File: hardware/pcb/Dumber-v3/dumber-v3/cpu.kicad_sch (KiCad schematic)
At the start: 25 parts, among them J1 Conn_02x03_Odd_Even, J2 Conn_02x03_Odd_Even, J3 Conn_02x05_Odd_Even, J4 TE 1-84982-0, M1 Motor, M2 Motor, Q2 PMN52XP, U1 XBEE-3, U2 STM32F071CBTx, U7 A3909

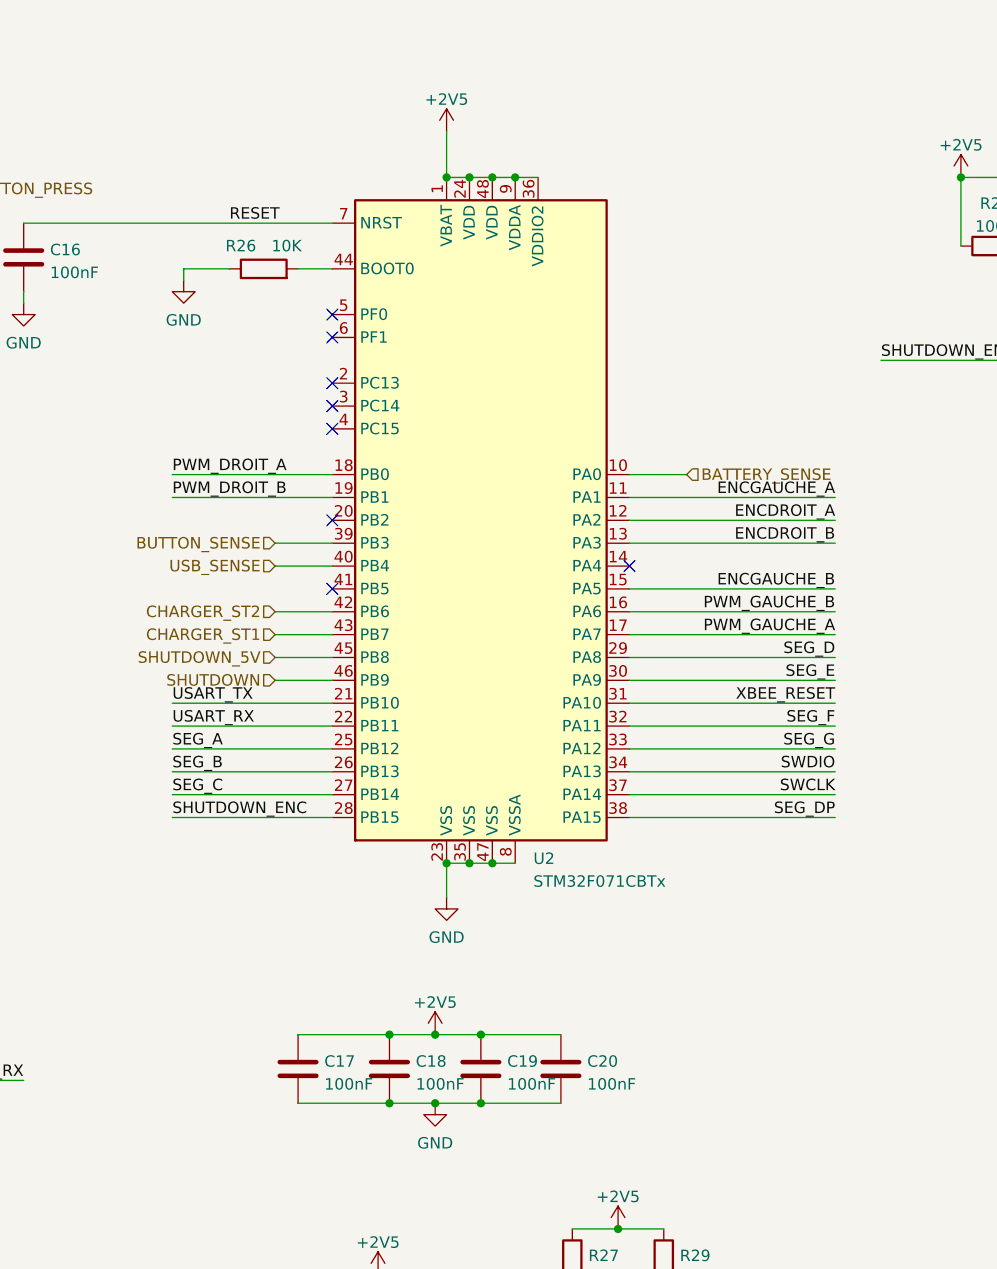
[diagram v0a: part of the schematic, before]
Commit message: Modifications after testing: func 11 needs more work.
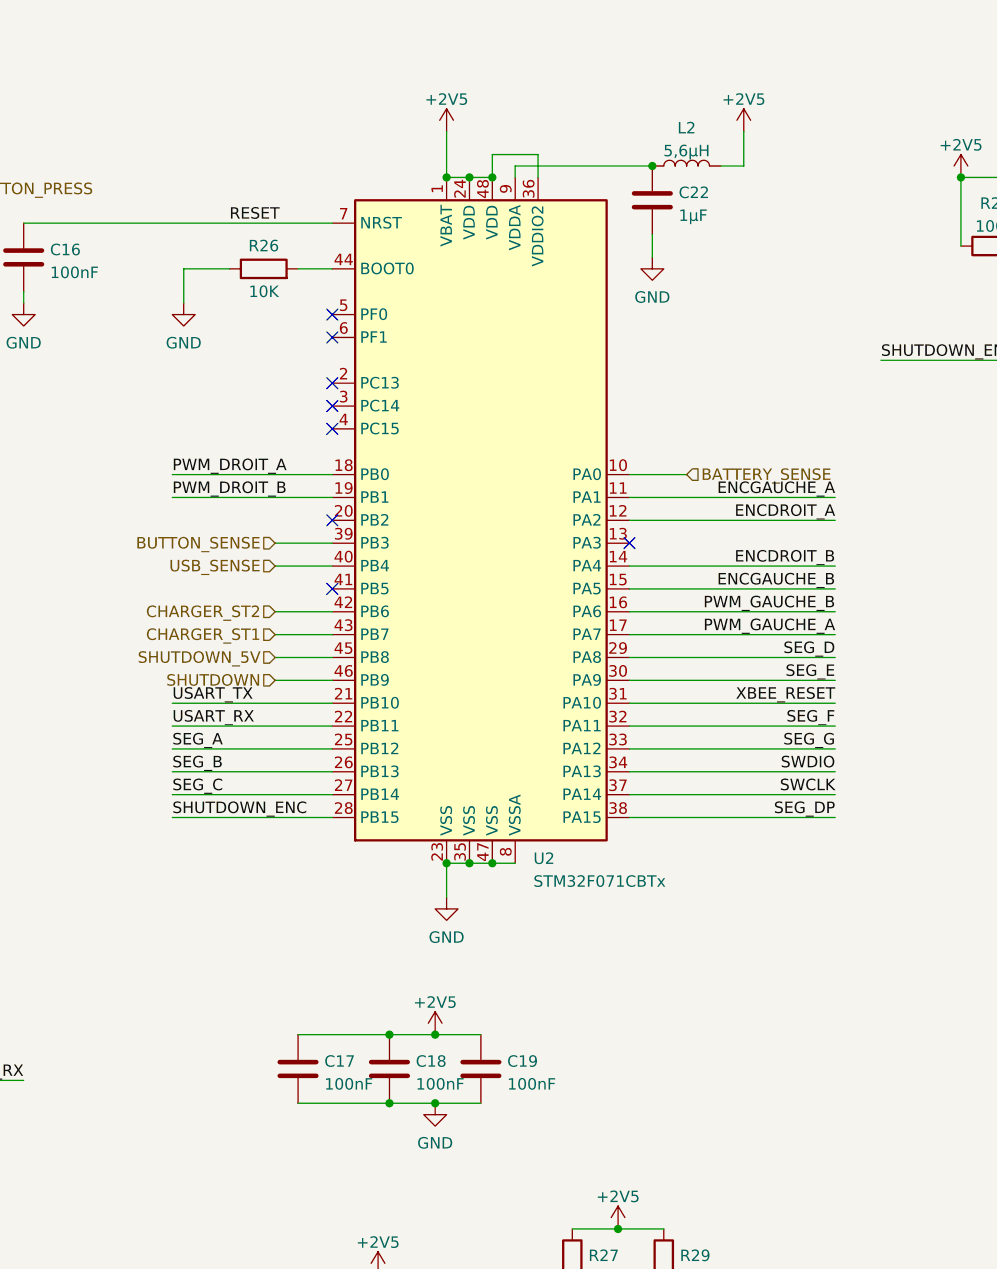
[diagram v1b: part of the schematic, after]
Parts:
- removed C20: 100nF, Capacitor_SMD:C_0805_2012Metric, symbol Device:C
- added C22: 1µF, Capacitor_SMD:C_0805_2012Metric, symbol Device:C
- added L2: 5,6µH, Inductor_SMD:L_1812_4532Metric, symbol Device:L
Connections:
- net +2V5: now also L2.2; no longer U2.9 (VDDA)
- net ENCDROIT_B: now also U2.14 (PA4); no longer U2.13 (PA3)
- net GND: now also C22.2
- new net: C22.1, L2.1, U2.9 (VDDA)
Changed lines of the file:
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@@
   (title_block
     (title "CPU + Com + Motors")
-    (date "2022-06-08")
-    (rev "1.0")
+    (date "2023-03-29")
+    (rev "2.1")
     (company "INSA - GEI")
   )
@@
   (junction (at 49.53 173.99) (diameter 0) (color 0 0 0 0)
   )
+  (junction (at 152.4 36.83) (diameter 0) (color 0 0 0 0)
+  )
   (junction (at 123.19 140.97) (diameter 0) (color 0 0 0 0)
   )
@@
   (junction (at 143.51 165.1) (diameter 0) (color 0 0 0 0)
   )
-  (junction (at 137.16 38.1) (diameter 0) (color 0 0 0 0)
-  )
   (junction (at 232.41 38.1) (diameter 0) (color 0 0 0 0)
   )
@@
   (junction (at 134.62 38.1) (diameter 0) (color 0 0 0 0)
   )
-  (junction (at 133.35 133.35) (diameter 0) (color 0 0 0 0)
-  )
-  (junction (at 133.35 140.97) (diameter 0) (color 0 0 0 0)
-  )
   (junction (at 128.27 133.35) (diameter 0) (color 0 0 0 0)
   )
@@
   )
   (no_connect (at 116.84 66.04))
-  (no_connect (at 149.86 81.28))
+  (no_connect (at 149.86 78.74))
   (no_connect (at 116.84 83.82))
   (no_connect (at 116.84 76.2))
@@
     (stroke (width 0) (type default) (color 0 0 0 0))
   )
+  (wire (pts (xy 134.62 38.1) (xy 134.62 35.56))
+    (stroke (width 0) (type default) (color 0 0 0 0))
+  )
   (wire (pts (xy 19.05 142.24) (xy 34.29 142.24))
     (stroke (width 0) (type default) (color 0 0 0 0))
@@
     (stroke (width 0) (type default) (color 0 0 0 0))
   )
+  (wire (pts (xy 139.7 35.56) (xy 139.7 38.1))
+    (stroke (width 0) (type default) (color 0 0 0 0))
+  )
   (wire (pts (xy 149.86 109.22) (xy 172.72 109.22))
     (stroke (width 0) (type default) (color 0 0 0 0))
@@
     (stroke (width 0) (type default) (color 0 0 0 0))
   )
+  (wire (pts (xy 134.62 35.56) (xy 139.7 35.56))
+    (stroke (width 0) (type default) (color 0 0 0 0))
+  )
+  (wire (pts (xy 162.56 33.02) (xy 162.56 36.83))
+    (stroke (width 0) (type default) (color 0 0 0 0))
+  )
   (wire (pts (xy 200.66 80.01) (xy 200.66 67.31))
     (stroke (width 0) (type default) (color 0 0 0 0))
   )
-  (wire (pts (xy 149.86 78.74) (xy 172.72 78.74))
-    (stroke (width 0) (type default) (color 0 0 0 0))
-  )
   (wire (pts (xy 64.77 138.43) (xy 82.55 138.43))
     (stroke (width 0) (type default) (color 0 0 0 0))
@@
     (stroke (width 0) (type default) (color 0 0 0 0))
   )
+  (wire (pts (xy 137.16 36.83) (xy 152.4 36.83))
+    (stroke (width 0) (type default) (color 0 0 0 0))
+  )
   (wire (pts (xy 217.17 45.72) (xy 234.95 45.72))
     (stroke (width 0) (type default) (color 0 0 0 0))
@@
     (stroke (width 0) (type default) (color 0 0 0 0))
   )
+  (wire (pts (xy 162.56 36.83) (xy 160.02 36.83))
+    (stroke (width 0) (type default) (color 0 0 0 0))
+  )
   (wire (pts (xy 266.7 92.71) (xy 266.7 96.52))
     (stroke (width 0) (type default) (color 0 0 0 0))
@@
     (stroke (width 0) (type default) (color 0 0 0 0))
   )
-  (wire (pts (xy 133.35 133.35) (xy 142.24 133.35))
-    (stroke (width 0) (type default) (color 0 0 0 0))
-  )
   (wire (pts (xy 54.61 39.37) (xy 54.61 69.85))
     (stroke (width 0) (type default) (color 0 0 0 0))
@@
     (stroke (width 0) (type default) (color 0 0 0 0))
   )
+  (wire (pts (xy 149.86 81.28) (xy 172.72 81.28))
+    (stroke (width 0) (type default) (color 0 0 0 0))
+  )
   (wire (pts (xy 129.54 33.02) (xy 129.54 38.1))
     (stroke (width 0) (type default) (color 0 0 0 0))
@@
     (stroke (width 0) (type default) (color 0 0 0 0))
   )
-  (wire (pts (xy 134.62 38.1) (xy 137.16 38.1))
-    (stroke (width 0) (type default) (color 0 0 0 0))
-  )
   (wire (pts (xy 201.93 38.1) (xy 232.41 38.1))
     (stroke (width 0) (type default) (color 0 0 0 0))
@@
     (stroke (width 0) (type default) (color 0 0 0 0))
   )
-  (wire (pts (xy 100.33 48.26) (xy 100.33 49.53))
+  (wire (pts (xy 100.33 48.26) (xy 100.33 52.07))
     (stroke (width 0) (type default) (color 0 0 0 0))
   )
@@
     (stroke (width 0) (type default) (color 0 0 0 0))
   )
-  (wire (pts (xy 133.35 140.97) (xy 142.24 140.97))
-    (stroke (width 0) (type default) (color 0 0 0 0))
-  )
   (wire (pts (xy 149.86 73.66) (xy 172.72 73.66))
     (stroke (width 0) (type default) (color 0 0 0 0))
@@
     (stroke (width 0) (type default) (color 0 0 0 0))
   )
+  (wire (pts (xy 152.4 44.45) (xy 152.4 46.99))
+    (stroke (width 0) (type default) (color 0 0 0 0))
+  )
   (wire (pts (xy 123.19 140.97) (xy 128.27 140.97))
     (stroke (width 0) (type default) (color 0 0 0 0))
   )
-  (wire (pts (xy 137.16 38.1) (xy 139.7 38.1))
-    (stroke (width 0) (type default) (color 0 0 0 0))
-  )
   (wire (pts (xy 113.03 48.26) (xy 116.84 48.26))
     (stroke (width 0) (type default) (color 0 0 0 0))
@@
     (stroke (width 0) (type default) (color 0 0 0 0))
   )
+  (wire (pts (xy 137.16 38.1) (xy 137.16 36.83))
+    (stroke (width 0) (type default) (color 0 0 0 0))
+  )
   (wire (pts (xy 232.41 29.21) (xy 234.95 29.21))
     (stroke (width 0) (type default) (color 0 0 0 0))
@@
     (stroke (width 0) (type default) (color 0 0 0 0))
   )
-  (label "ENCDROIT_B" (at 172.72 78.74 180)
+  (label "ENCDROIT_B" (at 172.72 81.28 180)
     (effects (font (size 1.27 1.27)) (justify right bottom))
   )
@@
     (effects (font (size 1.27 1.27)) (justify right))
   )
-  (symbol (lib_id "power:GND") (at 100.33 49.53 0) (unit 1)
-    (in_bom yes) (on_board yes) (fields_autoplaced)
-    (property "Reference" "#PWR030" (id 0) (at 100.33 55.88 0)
-      (effects (font (size 1.27 1.27)) hide)
-    )
-    (property "Value" "GND" (id 1) (at 100.33 53.9734 0))
-    (property "Footprint" "" (id 2) (at 100.33 49.53 0)
-      (effects (font (size 1.27 1.27)) hide)
-    )
-    (property "Datasheet" "" (id 3) (at 100.33 49.53 0)
+  (symbol (lib_id "power:GND") (at 100.33 52.07 0) (unit 1)
+    (in_bom yes) (on_board yes) (fields_autoplaced)
+    (property "Reference" "#PWR030" (id 0) (at 100.33 58.42 0)
+      (effects (font (size 1.27 1.27)) hide)
+    )
+    (property "Value" "GND" (id 1) (at 100.33 56.5134 0))
+    (property "Footprint" "" (id 2) (at 100.33 52.07 0)
+      (effects (font (size 1.27 1.27)) hide)
+    )
+    (property "Datasheet" "" (id 3) (at 100.33 52.07 0)
       (effects (font (size 1.27 1.27)) hide)
     )
@@
     (pin "1")
   )
+  (symbol (lib_id "Device:L") (at 156.21 36.83 90) (unit 1)
+    (in_bom yes) (on_board yes) (fields_autoplaced)
+    (property "Reference" "L2" (id 0) (at 156.21 32.6222 90))
+    (property "Value" "5,6µH" (id 1) (at 156.21 35.1591 90))
+    (property "Footprint" "Inductor_SMD:L_1812_4532Metric" (id 2) (at 156.21 36.83 0)
+      (effects (font (size 1.27 1.27)) hide)
+    )
+    (property "Datasheet" "~" (id 3) (at 156.21 36.83 0)
+      (effects (font (size 1.27 1.27)) hide)
+    )
+    (pin "1")
+    (pin "2")
+  )
   (symbol (lib_id "power:+2V5") (at 49.53 129.54 0) (unit 1)
     (in_bom yes) (on_board yes) (fields_autoplaced)
@@
     (pin "2")
   )
+  (symbol (lib_id "power:+2V5") (at 162.56 33.02 0) (unit 1)
+    (in_bom yes) (on_board yes) (fields_autoplaced)
+    (property "Reference" "#PWR035" (id 0) (at 162.56 36.83 0)
+      (effects (font (size 1.27 1.27)) hide)
+    )
+    (property "Value" "+2V5" (id 1) (at 162.56 29.4442 0))
+    (property "Footprint" "" (id 2) (at 162.56 33.02 0)
+      (effects (font (size 1.27 1.27)) hide)
+    )
+    (property "Datasheet" "" (id 3) (at 162.56 33.02 0)
+      (effects (font (size 1.27 1.27)) hide)
+    )
+    (pin "1")
+  )
   (symbol (lib_id "power:GND") (at 49.53 175.26 0) (unit 1)
     (in_bom yes) (on_board yes) (fields_autoplaced)
@@
     (pin "1")
   )
-  (symbol (lib_id "Device:C") (at 142.24 137.16 0) (unit 1)
-    (in_bom yes) (on_board yes) (fields_autoplaced)
-    (property "Reference" "C20" (id 0) (at 145.161 136.3253 0)
-      (effects (font (size 1.27 1.27)) (justify left))
-    )
-    (property "Value" "100nF" (id 1) (at 145.161 138.8622 0)
-      (effects (font (size 1.27 1.27)) (justify left))
-    )
-    (property "Footprint" "Capacitor_SMD:C_0805_2012Metric" (id 2) (at 143.2052 140.97 0)
-      (effects (font (size 1.27 1.27)) hide)
-    )
-    (property "Datasheet" "~" (id 3) (at 142.24 137.16 0)
-      (effects (font (size 1.27 1.27)) hide)
-    )
-    (pin "1")
-    (pin "2")
-  )
   (symbol (lib_id "Device:C") (at 82.55 46.99 0) (unit 1)
     (in_bom yes) (on_board yes) (fields_autoplaced)
@@
   (symbol (lib_id "Device:R") (at 109.22 48.26 90) (unit 1)
     (in_bom yes) (on_board yes)
-    (property "Reference" "R26" (id 0) (at 106.68 45.72 90))
-    (property "Value" "10K" (id 1) (at 111.76 45.72 90))
+    (property "Reference" "R26" (id 0) (at 109.22 45.72 90))
+    (property "Value" "10K" (id 1) (at 109.22 50.8 90))
     (property "Footprint" "Resistor_SMD:R_0805_2012Metric" (id 2) (at 109.22 50.038 90)
       (effects (font (size 1.27 1.27)) hide)
@@
     (pin "2")
   )
+  (symbol (lib_id "Device:C") (at 152.4 40.64 0) (unit 1)
+    (in_bom yes) (on_board yes) (fields_autoplaced)
+    (property "Reference" "C22" (id 0) (at 155.321 39.8053 0)
+      (effects (font (size 1.27 1.27)) (justify left))
+    )
+    (property "Value" "1µF" (id 1) (at 155.321 42.3422 0)
+      (effects (font (size 1.27 1.27)) (justify left))
+    )
+    (property "Footprint" "Capacitor_SMD:C_0805_2012Metric" (id 2) (at 153.3652 44.45 0)
+      (effects (font (size 1.27 1.27)) hide)
+    )
+    (property "Datasheet" "~" (id 3) (at 152.4 40.64 0)
+      (effects (font (size 1.27 1.27)) hide)
+    )
+    (pin "1")
+    (pin "2")
+  )
+  (symbol (lib_id "power:GND") (at 152.4 46.99 0) (unit 1)
+    (in_bom yes) (on_board yes) (fields_autoplaced)
+    (property "Reference" "#PWR029" (id 0) (at 152.4 53.34 0)
+      (effects (font (size 1.27 1.27)) hide)
+    )
+    (property "Value" "GND" (id 1) (at 152.4 51.4334 0))
+    (property "Footprint" "" (id 2) (at 152.4 46.99 0)
+      (effects (font (size 1.27 1.27)) hide)
+    )
+    (property "Datasheet" "" (id 3) (at 152.4 46.99 0)
+      (effects (font (size 1.27 1.27)) hide)
+    )
+    (pin "1")
+  )
   (symbol (lib_id "Connector_Generic:Conn_01x10") (at 45.72 34.29 90) (unit 1)
